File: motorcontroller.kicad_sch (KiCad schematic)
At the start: 44 parts

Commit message: Annotate schematic
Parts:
- gave numbers to parts that had none: 44

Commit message: Clean up BOM
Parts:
- H101, H102, H103, H104, H105, H106, H107, H108, H109, H110, J101, J103, J104, J105, J106, J107, J108, J109, J110, J111, J112: now left out of the parts list
- R104, R105, R107, R108, R111: value 10K -> 10k
- R106, R109: value 4.7K -> 4.7k

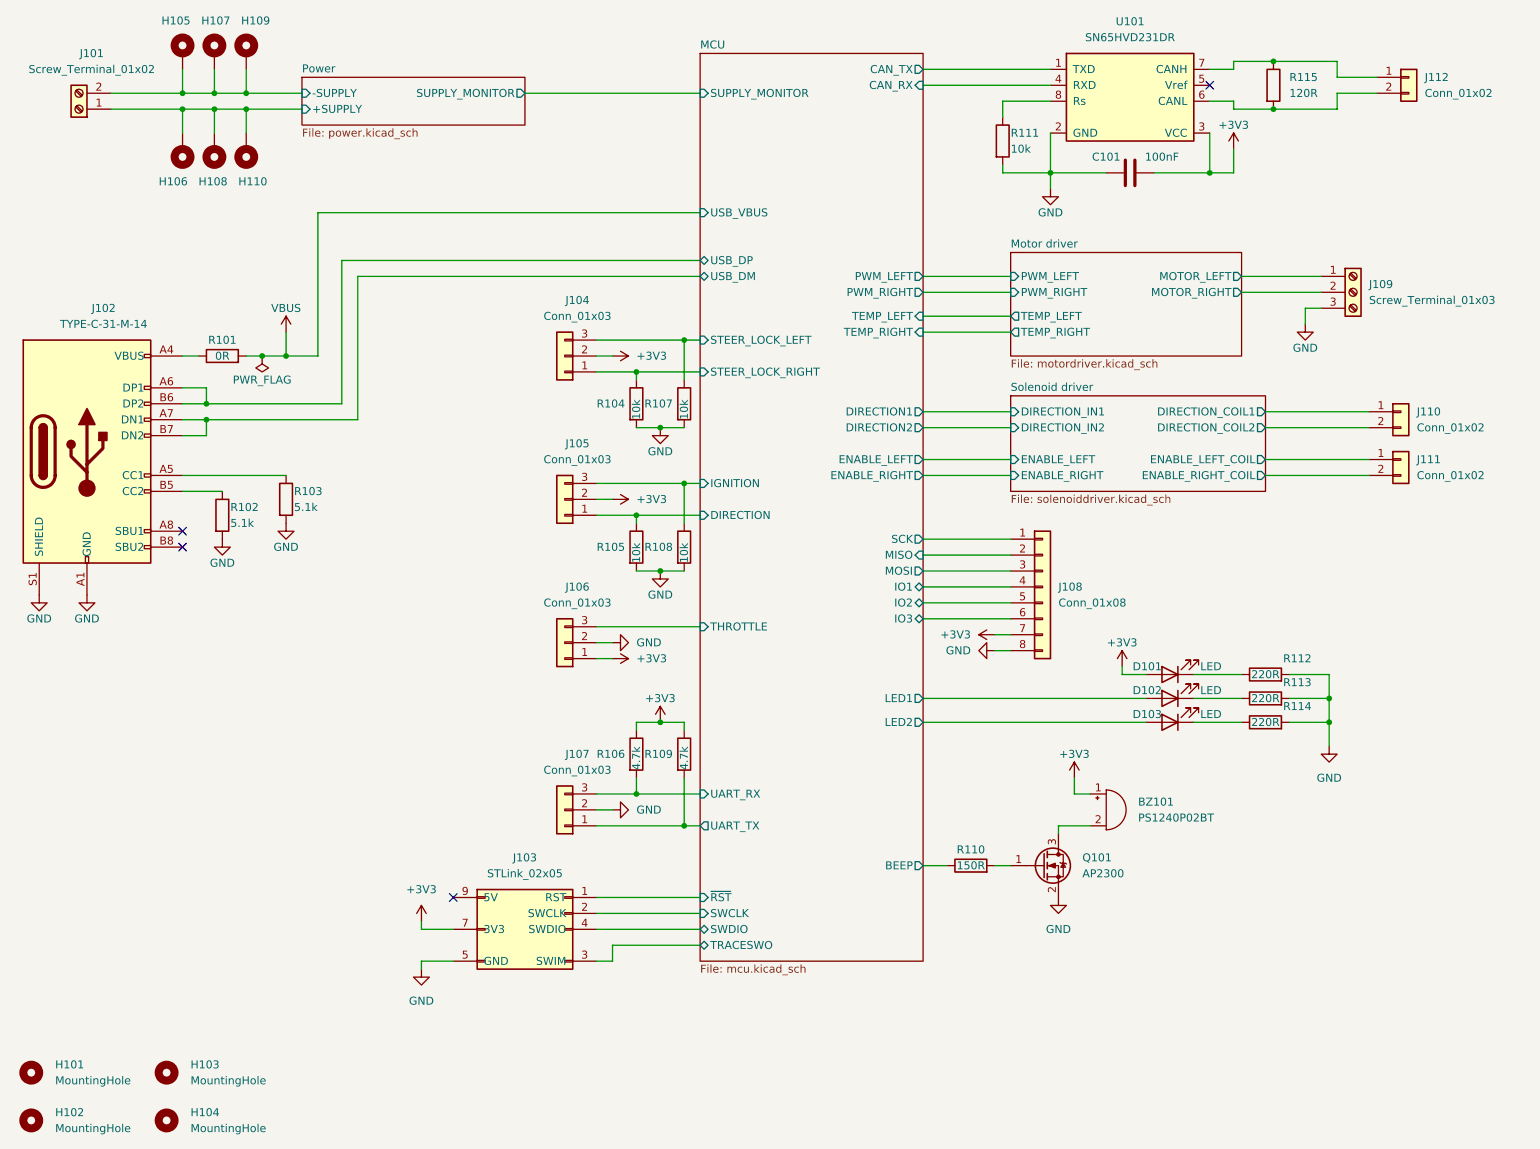
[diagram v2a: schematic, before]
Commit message: Assign footprints
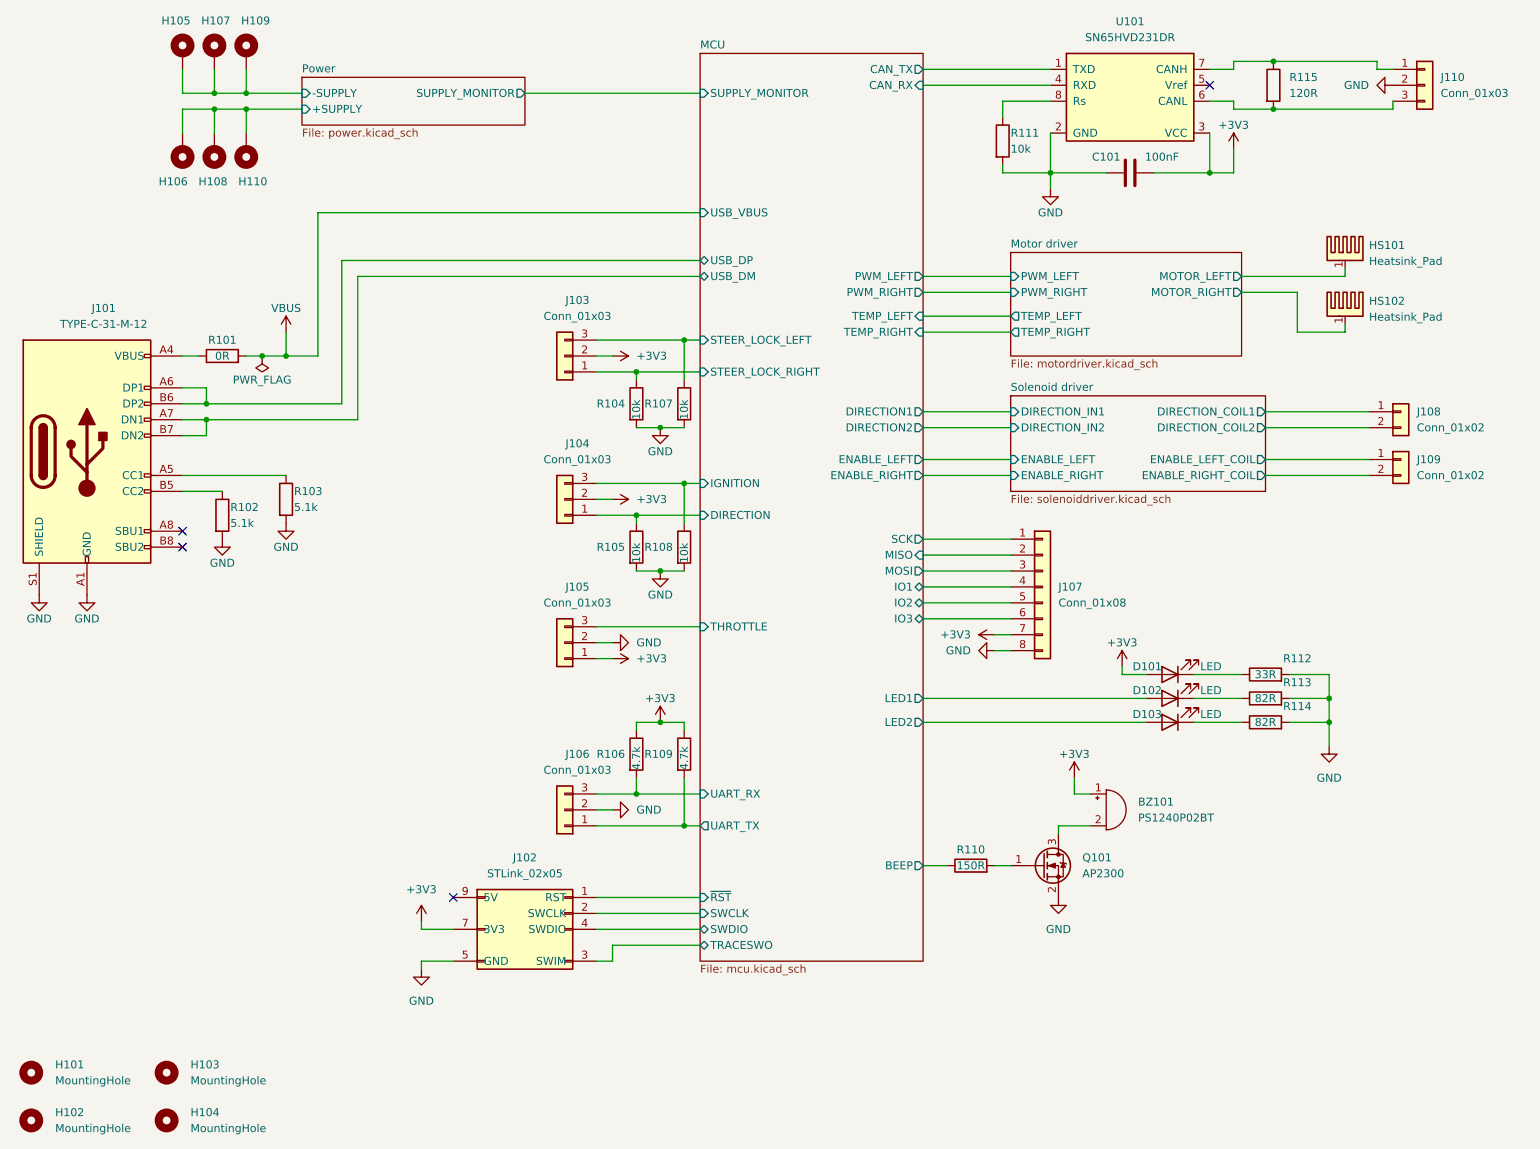
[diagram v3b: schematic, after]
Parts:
- removed J101: Screw_Terminal_01x02, symbol Connector:Screw_Terminal_01x02
- removed J102: TYPE-C-31-M-14, symbol GozLib:TYPE-C-31-M-14
- removed J109: Screw_Terminal_01x03, symbol Connector:Screw_Terminal_01x03
- removed J112: Conn_01x02, symbol Connector_Generic:Conn_01x02
- added HS101, HS102: Heatsink_Pad, symbol Mechanical:Heatsink_Pad
- added J101: TYPE-C-31-M-12, Connector_USB:USB_C_Receptacle_HRO_TYPE-C-31-M-12, symbol GozLib:TYPE-C-31-M-12
- added J110: Conn_01x03, Connector_JST:JST_XH_B3B-XH-A_1x03_P2.50mm_Vertical, symbol Connector_Generic:Conn_01x03
- BZ101: footprint (none) -> Buzzer_Beeper:Buzzer_TDK_PS1240P02BT_D12.2mm_H6.5mm
- C101: footprint (none) -> Capacitor_SMD:C_0805_2012Metric_Pad1.18x1.45mm_HandSolder
- D101, D102, D103: footprint (none) -> LED_SMD:LED_0805_2012Metric_Pad1.15x1.40mm_HandSolder
- H101, H102, H103, H104: footprint (none) -> MountingHole:MountingHole_4.3mm_M4
- H105, H106, H107, H108, H109, H110: footprint (none) -> MountingHole:MountingHole_4.3mm_M4_Pad
- J102: renamed from J103; footprint (none) -> Connector_PinHeader_2.54mm:PinHeader_2x05_P2.54mm_Vertical
- J103: renamed from J104; footprint (none) -> Connector_JST:JST_XH_B3B-XH-A_1x03_P2.50mm_Vertical
- J104: renamed from J105; footprint (none) -> Connector_JST:JST_XH_B3B-XH-A_1x03_P2.50mm_Vertical
- J105: renamed from J106; footprint (none) -> Connector_JST:JST_XH_B3B-XH-A_1x03_P2.50mm_Vertical
- J106: renamed from J107; footprint (none) -> Connector_PinHeader_2.54mm:PinHeader_1x03_P2.54mm_Vertical
- J107: renamed from J108; footprint (none) -> Connector_PinHeader_2.54mm:PinHeader_1x08_P2.54mm_Vertical
- J108: renamed from J110; footprint (none) -> Connector_JST:JST_XH_B2B-XH-A_1x02_P2.50mm_Vertical
- J109: renamed from J111; footprint (none) -> Connector_JST:JST_XH_B2B-XH-A_1x02_P2.50mm_Vertical
- Q101: footprint (none) -> Package_TO_SOT_SMD:TSOT-23_HandSoldering
- R101, R102, R103, R104, R105, R106, R107, R108, R109, R110, R111, R115: footprint (none) -> Resistor_SMD:R_0805_2012Metric_Pad1.20x1.40mm_HandSolder
- R112: value 220R -> 33R; footprint (none) -> Resistor_SMD:R_0805_2012Metric_Pad1.20x1.40mm_HandSolder
- R113, R114: value 220R -> 82R; footprint (none) -> Resistor_SMD:R_0805_2012Metric_Pad1.20x1.40mm_HandSolder
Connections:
- net GND: now also J101.A1 (GND), J101.A12 (GND), J101.B1 (GND), J101.B12 (GND), J101.S1 (SHIELD), J110.2 (Pin_2)
- net MCU/USB_DM: now also J101.A7 (DN1), J101.B7 (DN2)
- net MCU/USB_DP: now also J101.A6 (DP1), J101.B6 (DP2)
- net Motor driver/MOTOR_LEFT: now also HS101.1
- net Motor driver/MOTOR_RIGHT: now also HS102.1
- net at R115.1, U101.7 (CANH): now also J110.1 (Pin_1)
- net at R115.2, U101.6 (CANL): now also J110.3 (Pin_3)
- net at R103.1: now also J101.A5 (CC1)
- net at R102.1: now also J101.B5 (CC2)
- net at R101.1: now also J101.A4 (VBUS), J101.A9 (VBUS), J101.B4 (VBUS), J101.B9 (VBUS)

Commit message: Start PCB
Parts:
- D101: value LED -> PWR
- D102: value LED -> LED1
- D103: value LED -> LED2
- J103: value Conn_01x03 -> STRLCK
- J104: value Conn_01x03 -> IGN
- J105: value Conn_01x03 -> THROTTLE
- J106: value Conn_01x03 -> UART
- J107: value Conn_01x08 -> IO
- J108: value Conn_01x02 -> DIR
- J109: value Conn_01x02 -> EN
- J110: value Conn_01x03 -> CAN
- R101, R102, R103, R104, R105, R106, R107, R108, R109, R110, R111, R112, R113, R114, R115: footprint Resistor_SMD:R_0805_2012Metric_Pad1.20x1.40mm_HandSolder -> Resistor_SMD:R_0603_1608Metric_Pad0.98x0.95mm_HandSolder

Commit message: First PCB commit
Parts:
- C101: footprint Capacitor_SMD:C_0805_2012Metric_Pad1.18x1.45mm_HandSolder -> Capacitor_SMD:C_0603_1608Metric_Pad1.08x0.95mm_HandSolder
- H101, H102, H103, H104: footprint MountingHole:MountingHole_4.3mm_M4 -> MountingHole:MountingHole_2.7mm_M2.5
- J103, J104, J105, J106, J107, J108, J109: now in the parts list
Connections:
- net Solenoid driver/DIRECTION_COIL1: now also J108.2 (Pin_2); no longer J108.1 (Pin_1)
- net Solenoid driver/DIRECTION_COIL2: now also J108.1 (Pin_1); no longer J108.2 (Pin_2)
- net Solenoid driver/ENABLE_LEFT_COIL: now also J109.2 (Pin_2); no longer J109.1 (Pin_1)
- net Solenoid driver/ENABLE_RIGHT_COIL: now also J109.1 (Pin_1); no longer J109.2 (Pin_2)

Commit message: Finish regulator layout
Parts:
- added R116: 10k, Resistor_SMD:R_0603_1608Metric_Pad0.98x0.95mm_HandSolder, symbol Device:R
- added TP101: VBUS, TestPoint:TestPoint_Pad_D2.0mm, symbol Connector:TestPoint
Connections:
- net GND: now also R116.2
- net MCU/THROTTLE: now also R116.1
- net VBUS: now also TP101.1
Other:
- moved on the sheet: J105

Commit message: Finish PCB
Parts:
- added H111, H112: MountingHole_Pad, MountingHole:MountingHole_4.3mm_M4_Pad, symbol Mechanical:MountingHole_Pad
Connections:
- net MCU/MOSI: now also J107.1 (Pin_1); no longer J107.3 (Pin_3)
- net MCU/SCK: now also J107.3 (Pin_3); no longer J107.1 (Pin_1)
- net Power/+SUPPLY: now also H112.1
- net Power/-SUPPLY: now also H111.1
- net MCU/USB_DM renamed MCU/USB_DN
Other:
- sheet MCU ports: added USB_DN; removed USB_DM
- moved on the sheet: H105, H106, H107, H108, H109, H110
